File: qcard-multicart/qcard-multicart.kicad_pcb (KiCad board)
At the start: 2 copper layers, 55 x 54.5 mm, 14 parts, among them J1 Conn_02x18_Top_Bottom, SW1 SW_DIP_x04, U1 MX29LV640EBTI-70G, U2 MIC5365-3.3YD5

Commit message: WIP
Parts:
- added RN1: 2K, reb-r-array:EXB2HV202JV, F.Cu at (113.8, 65.8)
- added RN2: 2K, reb-r-array:EXB2HV202JV, F.Cu at (84.9, 65.8)
- added RN3: 2K, reb-r-array:EXB2HV202JV, F.Cu at (104.2, 65.8)
- added RN4: 2K, reb-r-array:EXB2HV202JV, F.Cu at (94.5, 65.8)
- moved U1 2.45 mm to (97.0, 55.5)
- renumbered REF** to M1, REF** to M2
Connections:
- J1 pad 10: /A3 -> Net-(J1-Pin_10)
- J1 pad 11: /A2 -> Net-(J1-Pin_11)
- J1 pad 12: /A1 -> Net-(J1-Pin_12)
- J1 pad 13: /A0 -> Net-(J1-Pin_13)
- J1 pad 14: /D0 -> Net-(J1-Pin_14)
- J1 pad 15: /D1 -> Net-(J1-Pin_15)
- J1 pad 16: /D2 -> Net-(J1-Pin_16)
- J1 pad 20: /A18 -> Net-(J1-Pin_20)
- J1 pad 21: /A17 -> Net-(J1-Pin_21)
- J1 pad 22: /A14 -> Net-(J1-Pin_22)
- J1 pad 23: /A13 -> Net-(J1-Pin_23)
- J1 pad 24: /A8 -> Net-(J1-Pin_24)
- J1 pad 25: /A9 -> Net-(J1-Pin_25)
- J1 pad 26: /A11 -> Net-(J1-Pin_26)
- J1 pad 27: /OE -> Net-(J1-Pin_27)
- J1 pad 28: /A10 -> Net-(J1-Pin_28)
- J1 pad 29: /CE -> Net-(J1-Pin_29)
- J1 pad 3: /A16 -> Net-(J1-Pin_3)
- J1 pad 30: /D7 -> Net-(J1-Pin_30)
- J1 pad 31: /D6 -> Net-(J1-Pin_31)
- J1 pad 32: /D5 -> Net-(J1-Pin_32)
- J1 pad 33: /D4 -> Net-(J1-Pin_33)
- J1 pad 34: /D3 -> Net-(J1-Pin_34)
- J1 pad 4: /A15 -> Net-(J1-Pin_4)
- J1 pad 5: /A12 -> Net-(J1-Pin_5)
- J1 pad 6: /A7 -> Net-(J1-Pin_6)
- J1 pad 7: /A6 -> Net-(J1-Pin_7)
- J1 pad 8: /A5 -> Net-(J1-Pin_8)
- J1 pad 9: /A4 -> Net-(J1-Pin_9)
- R2 pad 2: Net-(U1-A18) -> Net-(U1-A21)
- R3 pad 2: Net-(U1-A19) -> Net-(U1-A20)
- R4 pad 2: Net-(U1-A20) -> Net-(U1-A19)
- R5 pad 2: Net-(U1-A21) -> Net-(U1-A18)
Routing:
- net /A17: track 40.2 -> 0.00 mm, vias 1 -> 0
- net /A10: track 30.7 -> 0.00 mm, vias 1 -> 0
- net /A16: track 28.6 -> 0.00 mm
- net /A15: track 26.7 -> 0.00 mm
- net /A14: track 26.3 -> 0.00 mm, vias 1 -> 0
- net /A0: track 26.1 -> 0.00 mm
- net /A11: track 25.9 -> 0.00 mm, vias 1 -> 0
- net /A12: track 25.3 -> 0.00 mm
- net /D4: track 24.9 -> 0.00 mm, vias 1 -> 0
- net /D5: track 24.7 -> 0.00 mm, vias 1 -> 0
- net /A13: track 24.6 -> 0.00 mm, vias 1 -> 0
- net /A3: track 24.0 -> 0.00 mm, vias 2 -> 0
- net /D7: track 23.9 -> 0.00 mm, vias 1 -> 0
- net /D6: track 23.6 -> 0.00 mm, vias 1 -> 0
- net /A2: track 23.3 -> 0.00 mm
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
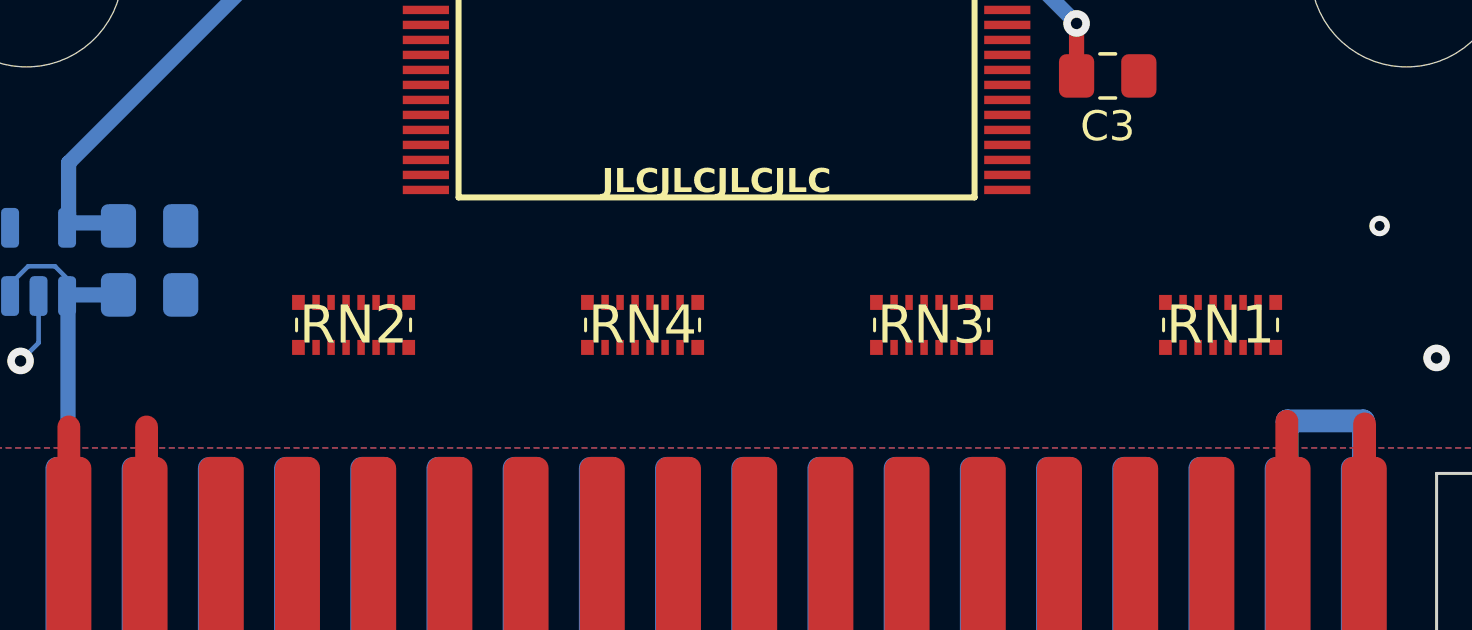
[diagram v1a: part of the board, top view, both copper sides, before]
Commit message: Adds staggered RNs (painstakingly)
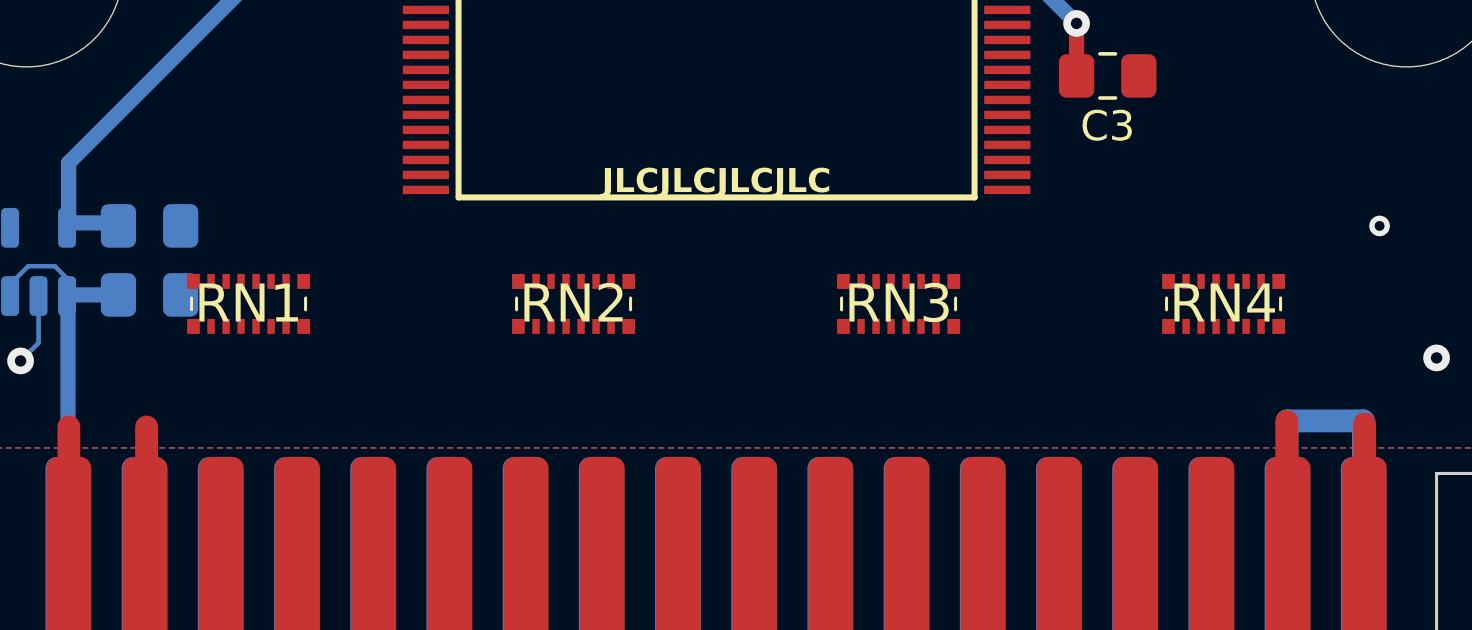
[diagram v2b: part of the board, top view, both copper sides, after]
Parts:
- moved RN1 32.4 mm to (81.4, 65.1)
- moved RN4 19.4 mm to (113.9, 65.1)
- moved RN2 7.37 mm to (92.2, 65.1), turned to 0 degrees
- moved RN3 1.30 mm to (103.1, 65.1)
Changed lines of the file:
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@@
   (net 81 "unconnected-(RN4-R8.2-Pad9)")
   (footprint "reb-r-array:EXB2HV202JV" (layer "F.Cu")
-    (at 113.8 65.8 180)
+    (at 81.4 65.1 180)
     (descr "EXB-2HV202JV-2")
     (tags "Resistor Network")
@@
   )
   (footprint "reb-r-array:EXB2HV202JV" (layer "F.Cu")
-    (at 104.166666 65.8 180)
+    (at 103.066666 65.1 180)
     (descr "EXB-2HV202JV-2")
     (tags "Resistor Network")
@@
   )
   (footprint "reb-r-array:EXB2HV202JV" (layer "F.Cu")
-    (at 84.9 65.8 180)
+    (at 92.233333 65.1)
     (descr "EXB-2HV202JV-2")
     (tags "Resistor Network")
@@
     (fp_line (start 1.9 0.8) (end -1.9 0.8)
       (stroke (width 0.2) (type solid)) (layer "F.Fab"))
-    (pad "1" smd rect (at -1.838 0.75 180) (size 0.425 0.5) (layers "F.Cu" "F.Paste" "F.Mask")
+    (pad "1" smd rect (at -1.838 0.75) (size 0.425 0.5) (layers "F.Cu" "F.Paste" "F.Mask")
       (net 52 "Net-(J1-Pin_8)") (pinfunction "R1.1") (pintype "passive"))
-    (pad "2" smd rect (at -1.25 0.75 180) (size 0.25 0.5) (layers "F.Cu" "F.Paste" "F.Mask")
+    (pad "2" smd rect (at -1.25 0.75) (size 0.25 0.5) (layers "F.Cu" "F.Paste" "F.Mask")
       (net 51 "Net-(J1-Pin_7)") (pinfunction "R2.1") (pintype "passive"))
-    (pad "3" smd rect (at -0.75 0.75 180) (size 0.25 0.5) (layers "F.Cu" "F.Paste" "F.Mask")
+    (pad "3" smd rect (at -0.75 0.75) (size 0.25 0.5) (layers "F.Cu" "F.Paste" "F.Mask")
       (net 50 "Net-(J1-Pin_6)") (pinfunction "R3.1") (pintype "passive"))
-    (pad "4" smd rect (at -0.25 0.75 180) (size 0.25 0.5) (layers "F.Cu" "F.Paste" "F.Mask")
+    (pad "4" smd rect (at -0.25 0.75) (size 0.25 0.5) (layers "F.Cu" "F.Paste" "F.Mask")
       (net 49 "Net-(J1-Pin_5)") (pinfunction "R4.1") (pintype "passive"))
-    (pad "5" smd rect (at 0.25 0.75 180) (size 0.25 0.5) (layers "F.Cu" "F.Paste" "F.Mask")
+    (pad "5" smd rect (at 0.25 0.75) (size 0.25 0.5) (layers "F.Cu" "F.Paste" "F.Mask")
       (net 48 "Net-(J1-Pin_4)") (pinfunction "R5.1") (pintype "passive"))
-    (pad "6" smd rect (at 0.75 0.75 180) (size 0.25 0.5) (layers "F.Cu" "F.Paste" "F.Mask")
+    (pad "6" smd rect (at 0.75 0.75) (size 0.25 0.5) (layers "F.Cu" "F.Paste" "F.Mask")
       (net 47 "Net-(J1-Pin_3)") (pinfunction "R6.1") (pintype "passive"))
-    (pad "7" smd rect (at 1.25 0.75 180) (size 0.25 0.5) (layers "F.Cu" "F.Paste" "F.Mask")
+    (pad "7" smd rect (at 1.25 0.75) (size 0.25 0.5) (layers "F.Cu" "F.Paste" "F.Mask")
       (net 76 "unconnected-(RN2-R7.1-Pad7)") (pinfunction "R7.1") (pintype "passive+no_connect"))
-    (pad "8" smd rect (at 1.838 0.75 180) (size 0.425 0.5) (layers "F.Cu" "F.Paste" "F.Mask")
+    (pad "8" smd rect (at 1.838 0.75) (size 0.425 0.5) (layers "F.Cu" "F.Paste" "F.Mask")
       (net 77 "unconnected-(RN2-R8.1-Pad8)") (pinfunction "R8.1") (pintype "passive+no_connect"))
-    (pad "9" smd rect (at 1.838 -0.75 180) (size 0.425 0.5) (layers "F.Cu" "F.Paste" "F.Mask")
+    (pad "9" smd rect (at 1.838 -0.75) (size 0.425 0.5) (layers "F.Cu" "F.Paste" "F.Mask")
       (net 78 "unconnected-(RN2-R8.2-Pad9)") (pinfunction "R8.2") (pintype "passive+no_connect"))
-    (pad "10" smd rect (at 1.25 -0.75 180) (size 0.25 0.5) (layers "F.Cu" "F.Paste" "F.Mask")
+    (pad "10" smd rect (at 1.25 -0.75) (size 0.25 0.5) (layers "F.Cu" "F.Paste" "F.Mask")
       (net 79 "unconnected-(RN2-R7.2-Pad10)") (pinfunction "R7.2") (pintype "passive+no_connect"))
-    (pad "11" smd rect (at 0.75 -0.75 180) (size 0.25 0.5) (layers "F.Cu" "F.Paste" "F.Mask")
+    (pad "11" smd rect (at 0.75 -0.75) (size 0.25 0.5) (layers "F.Cu" "F.Paste" "F.Mask")
       (net 1 "/A16") (pinfunction "R6.2") (pintype "passive"))
-    (pad "12" smd rect (at 0.25 -0.75 180) (size 0.25 0.5) (layers "F.Cu" "F.Paste" "F.Mask")
+    (pad "12" smd rect (at 0.25 -0.75) (size 0.25 0.5) (layers "F.Cu" "F.Paste" "F.Mask")
       (net 2 "/A15") (pinfunction "R5.2") (pintype "passive"))
-    (pad "13" smd rect (at -0.25 -0.75 180) (size 0.25 0.5) (layers "F.Cu" "F.Paste" "F.Mask")
+    (pad "13" smd rect (at -0.25 -0.75) (size 0.25 0.5) (layers "F.Cu" "F.Paste" "F.Mask")
       (net 5 "/A12") (pinfunction "R4.2") (pintype "passive"))
-    (pad "14" smd rect (at -0.75 -0.75 180) (size 0.25 0.5) (layers "F.Cu" "F.Paste" "F.Mask")
+    (pad "14" smd rect (at -0.75 -0.75) (size 0.25 0.5) (layers "F.Cu" "F.Paste" "F.Mask")
       (net 15 "/A7") (pinfunction "R3.2") (pintype "passive"))
-    (pad "15" smd rect (at -1.25 -0.75 180) (size 0.25 0.5) (layers "F.Cu" "F.Paste" "F.Mask")
+    (pad "15" smd rect (at -1.25 -0.75) (size 0.25 0.5) (layers "F.Cu" "F.Paste" "F.Mask")
       (net 16 "/A6") (pinfunction "R2.2") (pintype "passive"))
-    (pad "16" smd rect (at -1.838 -0.75 180) (size 0.425 0.5) (layers "F.Cu" "F.Paste" "F.Mask")
+    (pad "16" smd rect (at -1.838 -0.75) (size 0.425 0.5) (layers "F.Cu" "F.Paste" "F.Mask")
       (net 17 "/A5") (pinfunction "R1.2") (pintype "passive"))
     (model "EXB-2HV202JV.stp"
@@
   )
   (footprint "reb-r-array:EXB2HV202JV" (layer "F.Cu")
-    (at 94.533333 65.8 180)
+    (at 113.9 65.1 180)
     (descr "EXB-2HV202JV-2")
     (tags "Resistor Network")

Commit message: WIP
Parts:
- C1, C2, R1, R2, R3, R4, R5, U2: moved to F.Cu
- J1: value Conn_02x18_Top_Bottom -> QChord_EdgeConnector
- moved R2 13.1 mm to (100.8, 40.4)
- moved R5 13.1 mm to (93.2, 40.4)
- moved R3 10.9 mm to (98.3, 40.4)
- moved R4 10.9 mm to (95.7, 40.4)
- moved R1 4.70 mm to (80.5, 54.5)
- moved C1 4.35 mm to (73.8, 64.7), turned to 180 degrees
- moved C2 4.35 mm to (73.8, 62.4), turned to 180 degrees
- moved U2 3.05 mm to (77.5, 63.6)
- moved RN4 2.72 mm to (111.2, 65.4), turned to 0 degrees
- moved RN1 2.32 mm to (83.7, 65.4), turned to 0 degrees
- moved C3 2.20 mm to (110.1, 55.3)
- moved RN3 1.08 mm to (102.0, 65.4), turned to 0 degrees
- moved RN2 0.70 mm to (92.9, 65.4)
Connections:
- net Net-(J1-Pin_30) renamed /C30
- net Net-(J1-Pin_7) renamed /C7
- J1 pad 10: Net-(J1-Pin_10) -> /C10
- J1 pad 11: Net-(J1-Pin_11) -> /C11
- J1 pad 12: Net-(J1-Pin_12) -> /C12
- J1 pad 13: Net-(J1-Pin_13) -> /C13
- J1 pad 14: Net-(J1-Pin_14) -> /C14
- J1 pad 15: Net-(J1-Pin_15) -> /C15
- J1 pad 16: Net-(J1-Pin_16) -> /C16
- J1 pad 20: Net-(J1-Pin_20) -> /C20
- J1 pad 21: Net-(J1-Pin_21) -> /C21
- J1 pad 22: Net-(J1-Pin_22) -> /C22
- J1 pad 23: Net-(J1-Pin_23) -> /C23
- J1 pad 24: Net-(J1-Pin_24) -> /C24
- J1 pad 25: Net-(J1-Pin_25) -> /C25
- J1 pad 26: Net-(J1-Pin_26) -> /C26
- J1 pad 27: Net-(J1-Pin_27) -> /C27
- J1 pad 28: Net-(J1-Pin_28) -> /C28
- J1 pad 29: Net-(J1-Pin_29) -> /C29
- J1 pad 3: Net-(J1-Pin_3) -> /C3
- J1 pad 31: Net-(J1-Pin_31) -> /C31
- J1 pad 32: Net-(J1-Pin_32) -> /C32
- J1 pad 33: Net-(J1-Pin_33) -> /C33
- J1 pad 34: Net-(J1-Pin_34) -> /C34
- J1 pad 4: Net-(J1-Pin_4) -> /C4
- J1 pad 5: Net-(J1-Pin_5) -> /C5
- J1 pad 6: Net-(J1-Pin_6) -> /C6
- J1 pad 8: Net-(J1-Pin_8) -> /C8
- J1 pad 9: Net-(J1-Pin_9) -> /C9
- RN1 pad 1: Net-(J1-Pin_16) -> /C20
- RN1 pad 10: /A3 -> /A13
- RN1 pad 11: /A2 -> /A12
- RN1 pad 12: /A1 -> /A14
- RN1 pad 13: /A0 -> /A15
- RN1 pad 14: /D0 -> /A17
- RN1 pad 15: /D1 -> /A16
- RN1 pad 16: /D2 -> /A18
- RN1 pad 2: Net-(J1-Pin_15) -> /C3
- RN1 pad 3: Net-(J1-Pin_14) -> /C21
- RN1 pad 4: Net-(J1-Pin_13) -> /C4
- RN1 pad 5: Net-(J1-Pin_12) -> /C22
- RN1 pad 6: Net-(J1-Pin_11) -> /C5
- RN1 pad 7: Net-(J1-Pin_10) -> /C23
- RN1 pad 8: Net-(J1-Pin_9) -> /C6
- RN1 pad 9: /A4 -> /A7
- RN2 pad 1: Net-(J1-Pin_8) -> /C24
- RN2 pad 10: unconnected-(RN2-R7.2-Pad10) -> /OE
- RN2 pad 11: /A16 -> /A4
- RN2 pad 12: /A15 -> /A11
- RN2 pad 13: /A12 -> /A5
- RN2 pad 14: /A7 -> /A9
- RN2 pad 16: /A5 -> /A8
- RN2 pad 3: Net-(J1-Pin_6) -> /C25
- RN2 pad 4: Net-(J1-Pin_5) -> /C8
- RN2 pad 5: Net-(J1-Pin_4) -> /C26
- RN2 pad 6: Net-(J1-Pin_3) -> /C9
- RN2 pad 7: unconnected-(RN2-R7.1-Pad7) -> /C27
- RN2 pad 8: unconnected-(RN2-R8.1-Pad8) -> /C10
- RN2 pad 9: unconnected-(RN2-R8.2-Pad9) -> /A3
- RN3 pad 1: Net-(J1-Pin_34) -> /C28
- RN3 pad 10: /A10 -> /D6
- RN3 pad 11: /CE -> /A0
- RN3 pad 13: /D6 -> /A1
- RN3 pad 14: /D5 -> /CE
- RN3 pad 15: /D4 -> /A2
- RN3 pad 16: /D3 -> /A10
- RN3 pad 2: Net-(J1-Pin_33) -> /C11
- RN3 pad 3: Net-(J1-Pin_32) -> /C29
- RN3 pad 4: Net-(J1-Pin_31) -> /C12
- RN3 pad 6: Net-(J1-Pin_29) -> /C13
- RN3 pad 7: Net-(J1-Pin_28) -> /C31
- RN3 pad 8: Net-(J1-Pin_27) -> /C14
- RN3 pad 9: /OE -> /D0
- RN4 pad 1: Net-(J1-Pin_26) -> /C32
- RN4 pad 10: /A18 -> unconnected-(RN4-R7.2-Pad10)
- RN4 pad 11: /A17 -> unconnected-(RN4-R6.2-Pad11)
- RN4 pad 12: /A14 -> /D3
- RN4 pad 13: /A13 -> /D2
- RN4 pad 14: /A8 -> /D4
- RN4 pad 15: /A9 -> /D1
- RN4 pad 16: /A11 -> /D5
- RN4 pad 2: Net-(J1-Pin_25) -> /C15
- RN4 pad 3: Net-(J1-Pin_24) -> /C33
- RN4 pad 4: Net-(J1-Pin_23) -> /C16
- RN4 pad 5: Net-(J1-Pin_22) -> /C34
- RN4 pad 6: Net-(J1-Pin_21) -> unconnected-(RN4-R6.1-Pad6)
- RN4 pad 7: Net-(J1-Pin_20) -> unconnected-(RN4-R7.1-Pad7)
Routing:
- net +3.3V: track 44.7 -> 0.00 mm, vias 1 -> 0
- net Net-(U1-A18): track 44.0 -> 0.00 mm, vias 0 -> 1
- net Net-(U1-A21): track 30.6 -> 0.00 mm
- net Net-(U1-A20): track 29.5 -> 0.00 mm
- net Net-(U1-A19): track 28.5 -> 0.00 mm
- net /A16: track 0.00 -> 18.4 mm
- net /A15: track 0.00 -> 16.5 mm
- net /C20: track 0.00 -> 16.2 mm, vias 0 -> 1
- net /A14: track 0.00 -> 15.8 mm
- net +5V: track 15.7 -> 0.00 mm
- net /A17: track 0.00 -> 15.0 mm, vias 0 -> 1
- net /A12: track 0.00 -> 14.6 mm
- net /C31: track 0.00 -> 12.6 mm, vias 0 -> 1
- net /C14: track 0.00 -> 12.1 mm
- net /A18: track 0.00 -> 11.8 mm, vias 0 -> 2
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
